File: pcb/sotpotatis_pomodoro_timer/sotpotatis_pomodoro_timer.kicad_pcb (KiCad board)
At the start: 4 copper layers, 85 x 68.2 mm, 48 parts, among them J1 GENERIC_PWR_IN, J2 USB_C_PWR_IN, SW1 RIGHT_BTN, SW2 PRESET_1_BTN, SW3 PRESET_2_BTN, SW4 PRESET_3_BTN, SW5 LEFT_BTN, SW6 PWR_SWITCH, U1 ATtiny84A-P

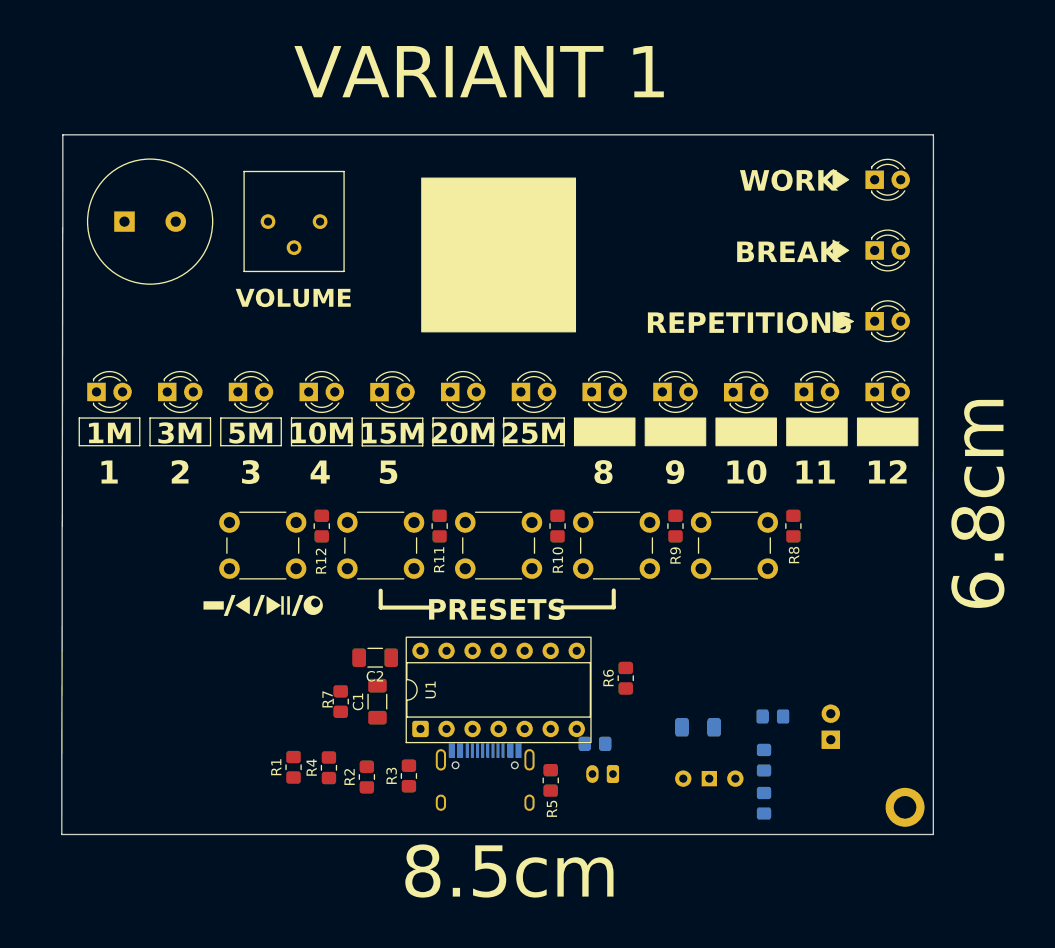
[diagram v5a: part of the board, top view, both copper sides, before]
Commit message: add: Layout variant 2 of PCB
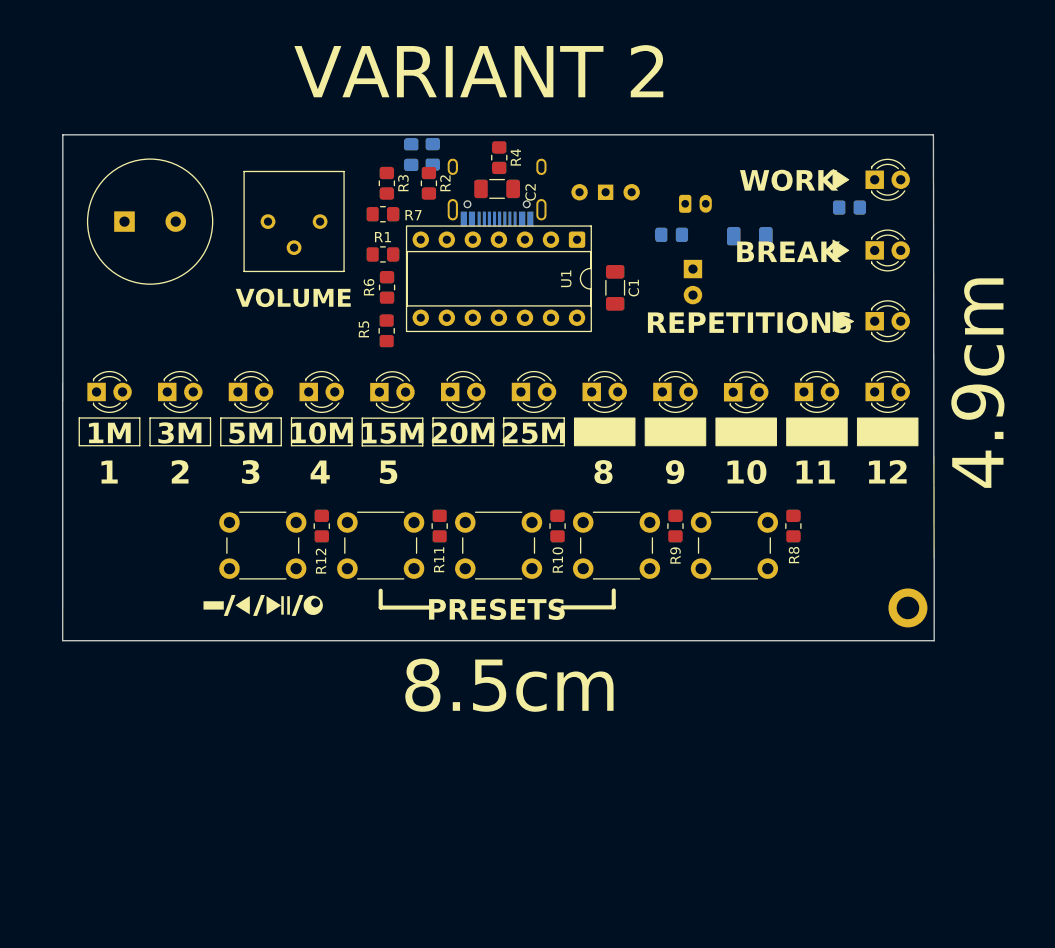
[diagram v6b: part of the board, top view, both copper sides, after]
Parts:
- moved R16 71.1 mm to (151.2, 98.9), turned to -90 degrees
- moved R14 68.4 mm to (149.1, 98.9), turned to -90 degrees
- moved R4 61.8 mm to (157.7, 99.2), turned to -90 degrees
- moved J2 59.9 mm to (157.5, 101.2), turned to 0 degrees
- moved R2 58.2 mm to (150.8, 101.7), turned to -90 degrees
- moved SW6 58.1 mm to (168.0, 102.6), turned to 0 degrees
- moved R15 57.9 mm to (191.8, 104.1), turned to 0 degrees
- moved R3 57.9 mm to (146.7, 101.7), turned to -90 degrees
- moved J1 56.1 mm to (175.8, 103.7), turned to 0 degrees
- moved R1 50.8 mm to (146.3, 108.7), turned to 0 degrees
- moved U1 50.1 mm to (165.2, 107.2), turned to -90 degrees
- moved C3 48.2 mm to (182.1, 106.9), turned to 0 degrees
- moved R13 48.0 mm to (174.5, 106.8), turned to 0 degrees
- moved D16 47.8 mm to (176.6, 110.1), turned to -90 degrees
- moved R7 47.7 mm to (146.3, 104.7), turned to 0 degrees
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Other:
- board size 85 x 68.2 mm -> 85 x 49.3 mm
- board text added: "4.9cm"
- board text added: "VARIANT 2"
- board text removed: "6.8cm"
- board text removed: "VARIANT 1"

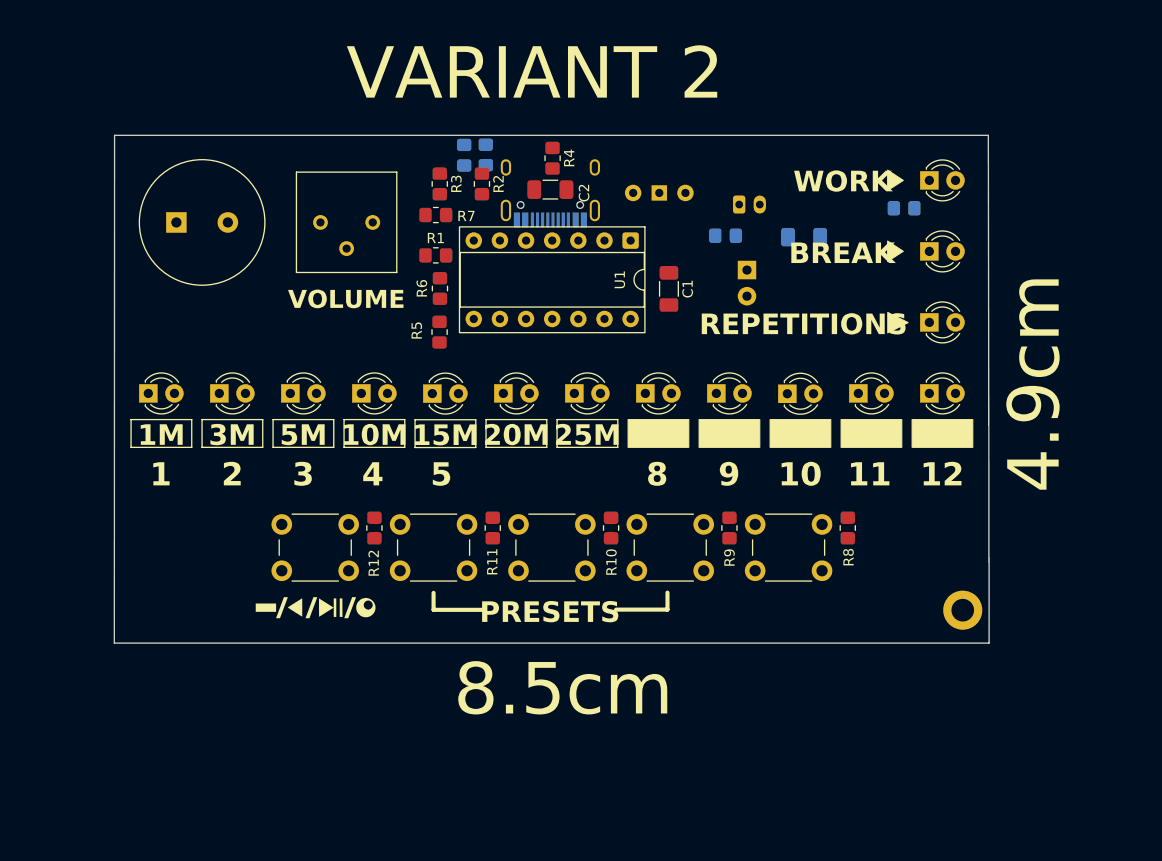
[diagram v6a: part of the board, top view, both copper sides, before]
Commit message: add: Layout variant 3 of PCB
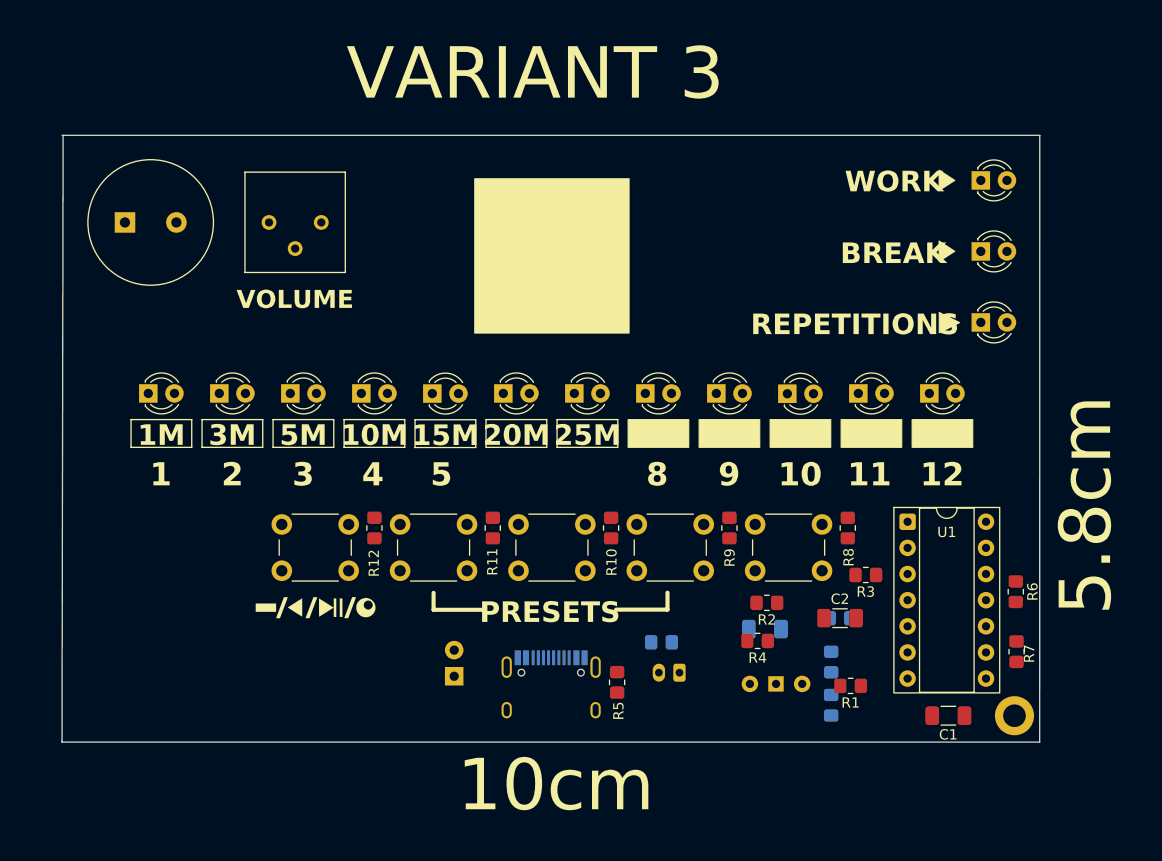
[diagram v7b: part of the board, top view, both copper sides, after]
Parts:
- moved R7 70.6 mm to (202.8, 147.2), turned to -90 degrees
- moved R6 63.2 mm to (202.7, 141.3)
- moved R16 63.1 mm to (184.7, 152.4), turned to 90 degrees
- moved R14 60.8 mm to (184.7, 148.2), turned to 90 degrees
- moved R1 58.1 mm to (186.6, 150.5), turned to 180 degrees
- moved R3 56.2 mm to (188.1, 139.7), turned to 180 degrees
- moved R4 51.0 mm to (177.6, 146.1), turned to 180 degrees
- moved J2 50.6 mm to (157.5, 151.8), turned to 180 degrees
- moved C2 50.3 mm to (185.6, 143.9), turned to 0 degrees
- moved C1 49.6 mm to (196.1, 153.4), turned to 180 degrees
- moved R2 49.2 mm to (178.5, 142.4), turned to 180 degrees
- moved SW6 49.0 mm to (179.4, 150.3), turned to 180 degrees
- moved D16 48.7 mm to (148.1, 149.6), turned to 90 degrees
- moved R15 48.3 mm to (168.2, 146.3), turned to 180 degrees
- moved J1 45.9 mm to (170.0, 149.2), turned to 180 degrees
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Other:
- board size 85 x 49.3 mm -> 95 x 59 mm
- board text added: "10cm"
- board text added: "5.8cm"
- board text added: "VARIANT 3"
- board text removed: "4.9cm"
- board text removed: "8.5cm"
- board text removed: "VARIANT 2"

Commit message: add: Backup progress with updated variant 1 PCB
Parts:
- added G***: LOGO, LOGO, F.Cu at (118.0, 162.7)
- added G***: LOGO, LOGO, F.Cu at (118.2, 150.6)
- added G***: LOGO, LOGO, F.Cu at (124.9, 185.7)
- added G***: LOGO, LOGO, F.Cu at (118.2, 141.4)
- added G***: LOGO, LOGO, F.Cu at (123.2, 181.0)
- added G***: LOGO, LOGO, F.Cu at (128.8, 191.3)
- added G***: LOGO, LOGO, F.Cu at (118.2, 171.1)
- added G***: LOGO, LOGO, F.Cu at (118.2, 145.9)
- added G***: LOGO, LOGO, F.Cu at (118.1, 156.0)
- added G***: LOGO, LOGO, F.Cu at (130.7, 115.8)
- BZ1: footprint custom-project-libraries:Buzzer_12x5.5RM0.6 -> custom-project-libraries:Buzzer_12x5.5RM6.5
- C1, C2, C3: footprint Capacitor_SMD:C_1206_3216Metric_Pad1.33x1.80mm_HandSolder -> Capacitor_SMD:C_0805_2012Metric_Pad1.18x1.45mm_HandSolder
- moved R7 96.0 mm to (116.7, 104.6), turned to 90 degrees
- moved C1 90.2 mm to (120.2, 104.7), turned to 90 degrees
- moved R1 84.4 mm to (112.0, 111.1), turned to 90 degrees
- moved C2 78.7 mm to (120.0, 100.4), turned to 180 degrees
- moved U1 73.0 mm to (124.4, 107.3), turned to 90 degrees
- moved R4 71.3 mm to (115.5, 111.1), turned to 90 degrees
- moved R3 70.5 mm to (123.3, 111.9), turned to 90 degrees
- moved R6 70.1 mm to (144.4, 102.4), turned to 90 degrees
- moved R2 66.6 mm to (119.2, 112.0), turned to 90 degrees
- moved D13 56.6 mm to (168.7, 53.7)
- moved D14 56.6 mm to (168.7, 60.6)
- moved D15 56.6 mm to (168.7, 67.5)
- moved D1 54.1 mm to (92.8, 74.4)
- moved D11 54.1 mm to (161.8, 74.4)
- moved D12 54.1 mm to (168.7, 74.4)
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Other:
- board size 95 x 59 mm -> 85 x 68.2 mm
- board text added: "1.25mm bold"
- board text added: "1.25mm not bold"
- board text added: "1.5mm bold"
- board text added: "1.5mm not bold"
- board text added: "12mm width"
- board text added: "16mm width"
- board text added: "1mm bold"
- board text added: "1mm not bold"
- board text added: "2.5mm bold"
- board text added: "2.5mm not bold"
- board text added: "24mm width"
- board text added: "2mm bold"
- board text added: "2mm not bold"
- board text added: "3mm bold"
- board text added: "3mm not bold"
- board text added: "6.8cm"
- board text added: "8.5cm"
- board text added: "OFF/ON"
- board text added: "SIZE TEST"
- board text added: "VARIANT 1"
- board text removed: "10cm"
- board text removed: "5.8cm"
- board text removed: "VARIANT 3"
